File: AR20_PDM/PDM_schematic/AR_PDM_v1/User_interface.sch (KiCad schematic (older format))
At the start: 63 parts, among them P1 B4B-PH-SM4-TB, U32 Fet-P, U33 Fet-P, U34 Fet-P, U35 Fet-P, U36 Fet-P

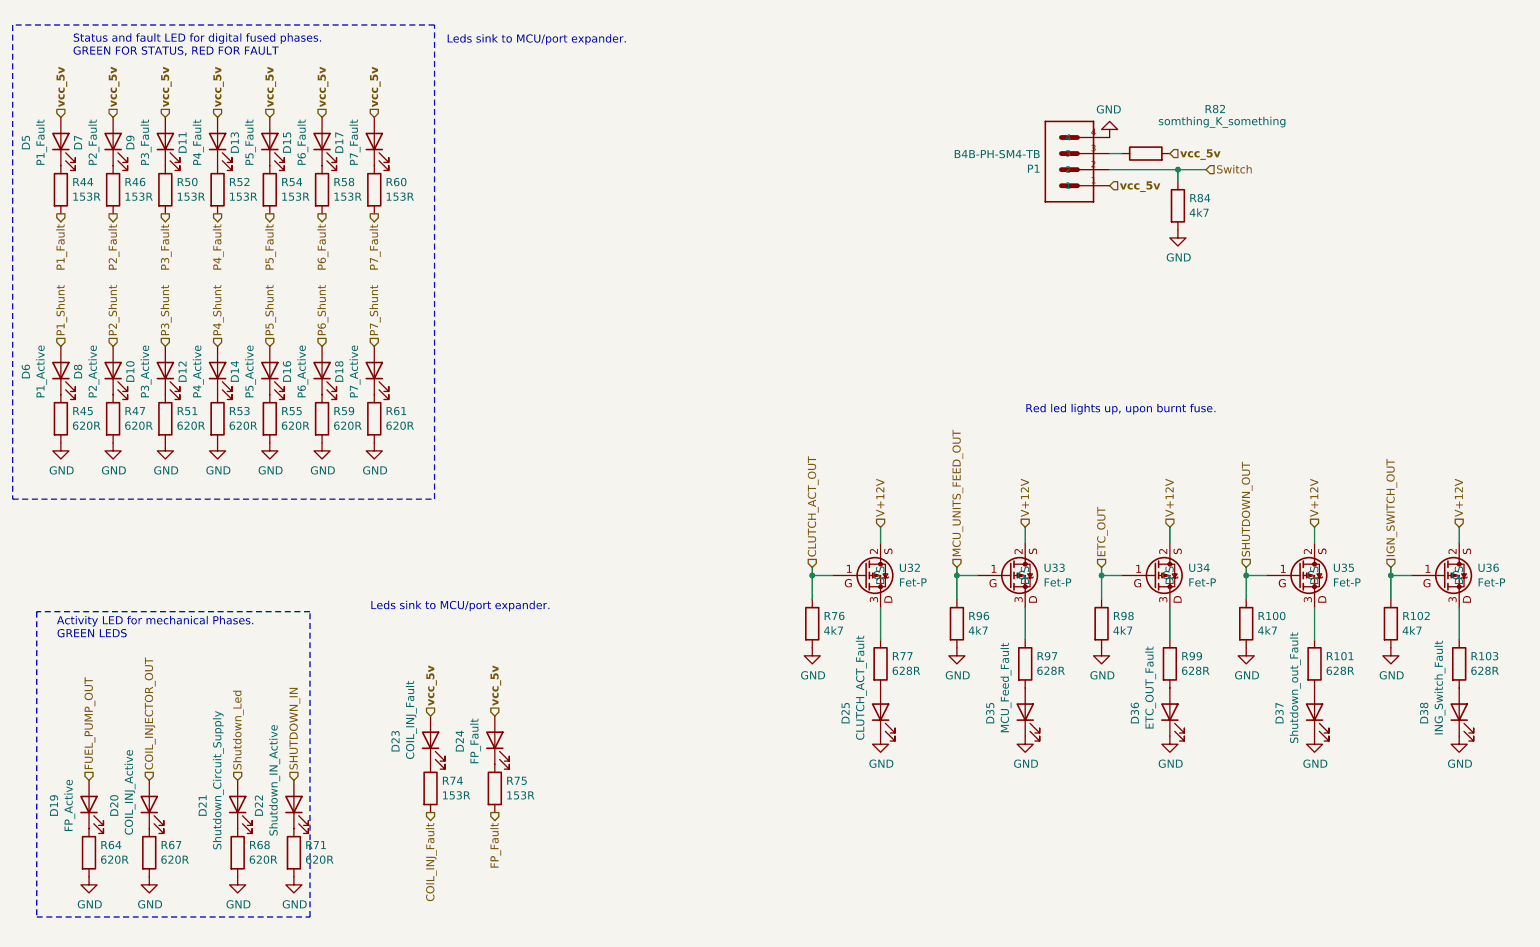
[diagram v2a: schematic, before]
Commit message: Further testing, reveals pdm needs rework
-  As of now, there are major errors in schematics.
- Needs rework. Version charlie postponed.
- Very nice pcb layout thats almost finished. 
   worth noting this layout for the future
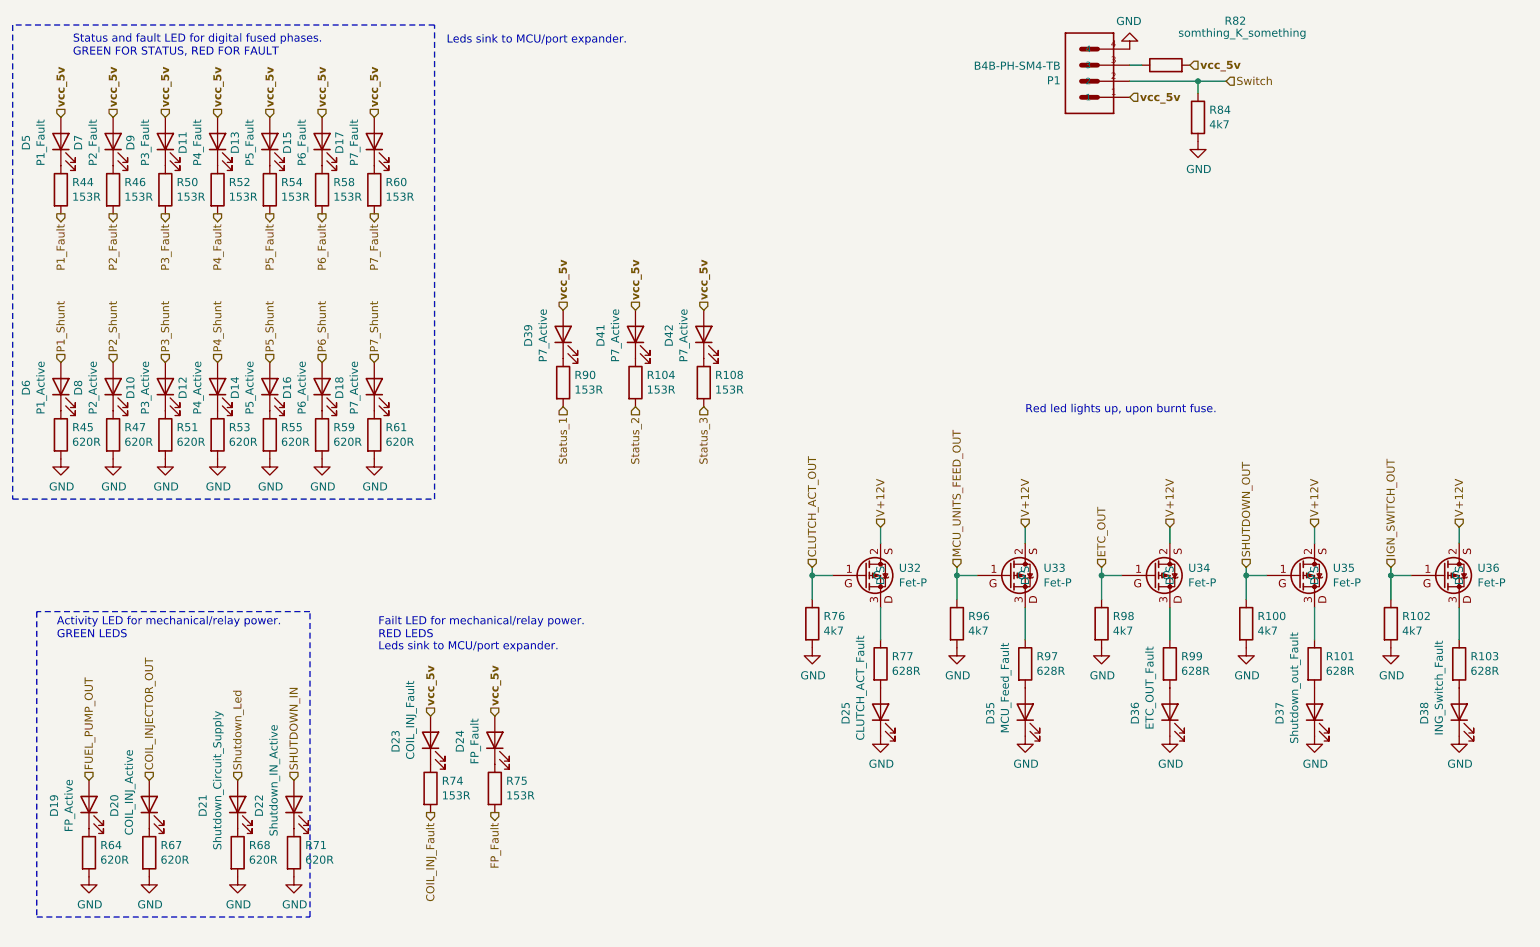
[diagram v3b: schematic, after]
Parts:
- added D39, D41, D42: P7_Active, LED_SMD:LED_1206_3216Metric, symbol Device:LED
- added R104, R108, R90: 153R, Resistor_SMD:R_0603_1608Metric, symbol AR20_PDM_v1-rescue:R-Device
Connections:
- net vcc_5v: now also D39.2 (A), D41.2 (A), D42.2 (A)
- new net: D39.1 (K), R90.1
- new net: D41.1 (K), R104.1
- new net: D42.1 (K), R108.1
- new net Status_1: R90.2
- new net Status_2: R104.2
- new net Status_3: R108.2
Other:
- note added: "Activity LED for mechanical/relay power.\nGREEN LEDS"
- note added: "Failt LED for mechanical/relay power.\nRED LEDS"
- note removed: "Activity LED for mechanical Phases. \nGREEN LEDS"
- moved on the sheet: D10, D12, D14, D16, D18, D6, D8, P1, R45, R47, R51, R53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

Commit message: Working on pcb layout
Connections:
- net P1_Shunt renamed P1_OUT
- net P2_Shunt renamed P2_OUT
- net P3_Shunt renamed P3_OUT
- net P4_Shunt renamed P4_OUT
- net P5_Shunt renamed P5_OUT
- net P6_Shunt renamed P6_OUT
- net P7_Shunt renamed P7_OUT
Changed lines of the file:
@@
 $EndComp
 Text HLabel 2175 3025 1    50   Input ~ 0
-P2_Shunt
+P2_OUT
 Text HLabel 2500 3025 1    50   Input ~ 0
-P3_Shunt
+P3_OUT
 Text HLabel 2825 3025 1    50   Input ~ 0
-P4_Shunt
+P4_OUT
 Text HLabel 3150 3025 1    50   Input ~ 0
-P5_Shunt
+P5_OUT
 Text HLabel 3475 3025 1    50   Input ~ 0
-P6_Shunt
+P6_OUT
 Text HLabel 3800 3025 1    50   Input ~ 0
-P7_Shunt
+P7_OUT
 Text HLabel 2950 5625 1    50   Input ~ 0
 Shutdown_Led
@@
 SHUTDOWN_IN
 Text HLabel 1850 3025 1    50   Input ~ 0
-P1_Shunt
+P1_OUT
 $Comp
 L AR20_PDM_v1-rescue:B4B-PH-SM4-TB P?

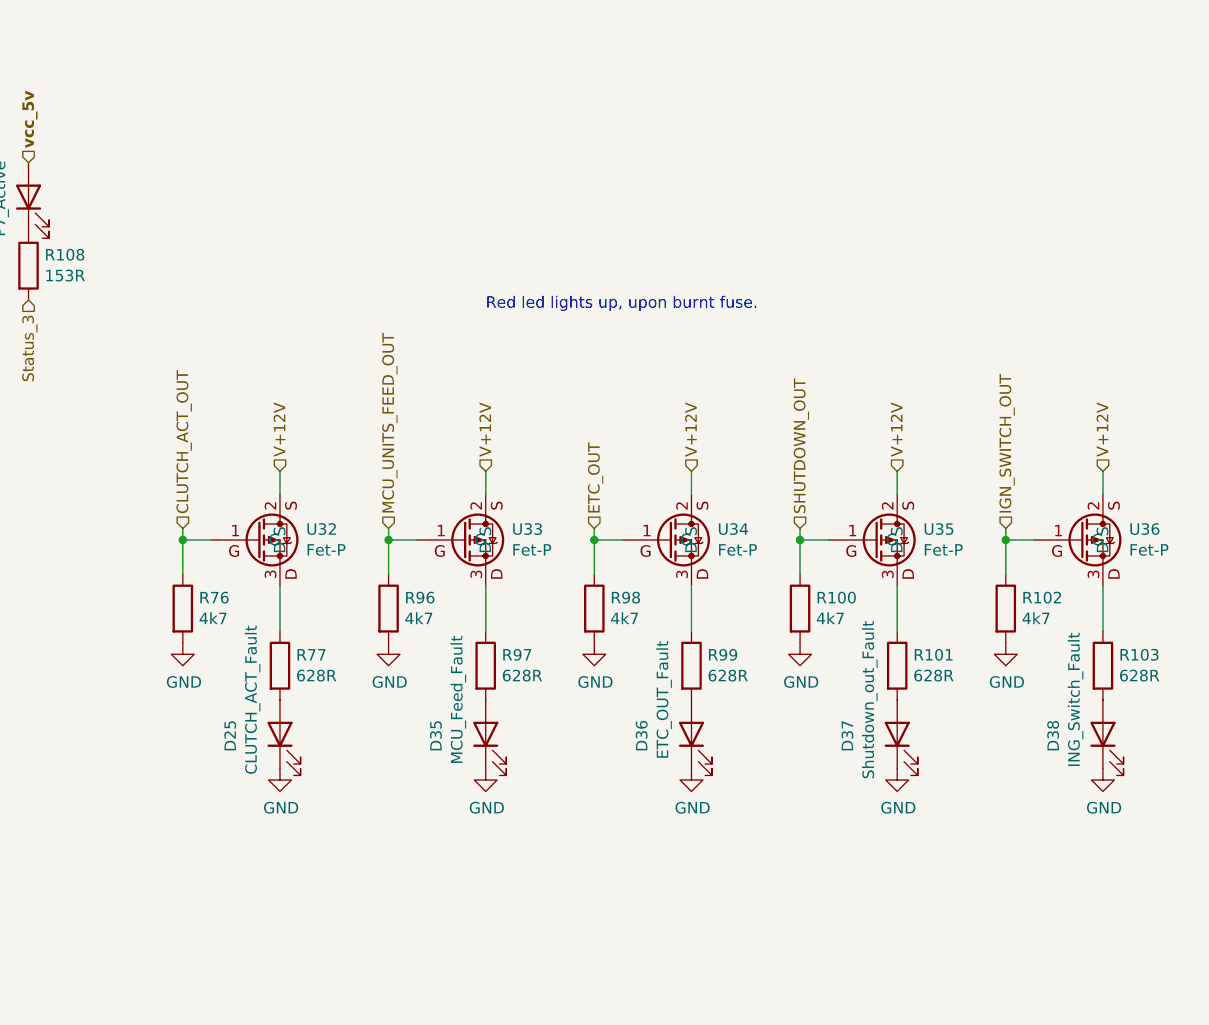
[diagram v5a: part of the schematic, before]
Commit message: PDM mostly complete
- Reverse polarity protection implemented
- All traces layed out
- final polish missing
- DRC missing
- Final check missing
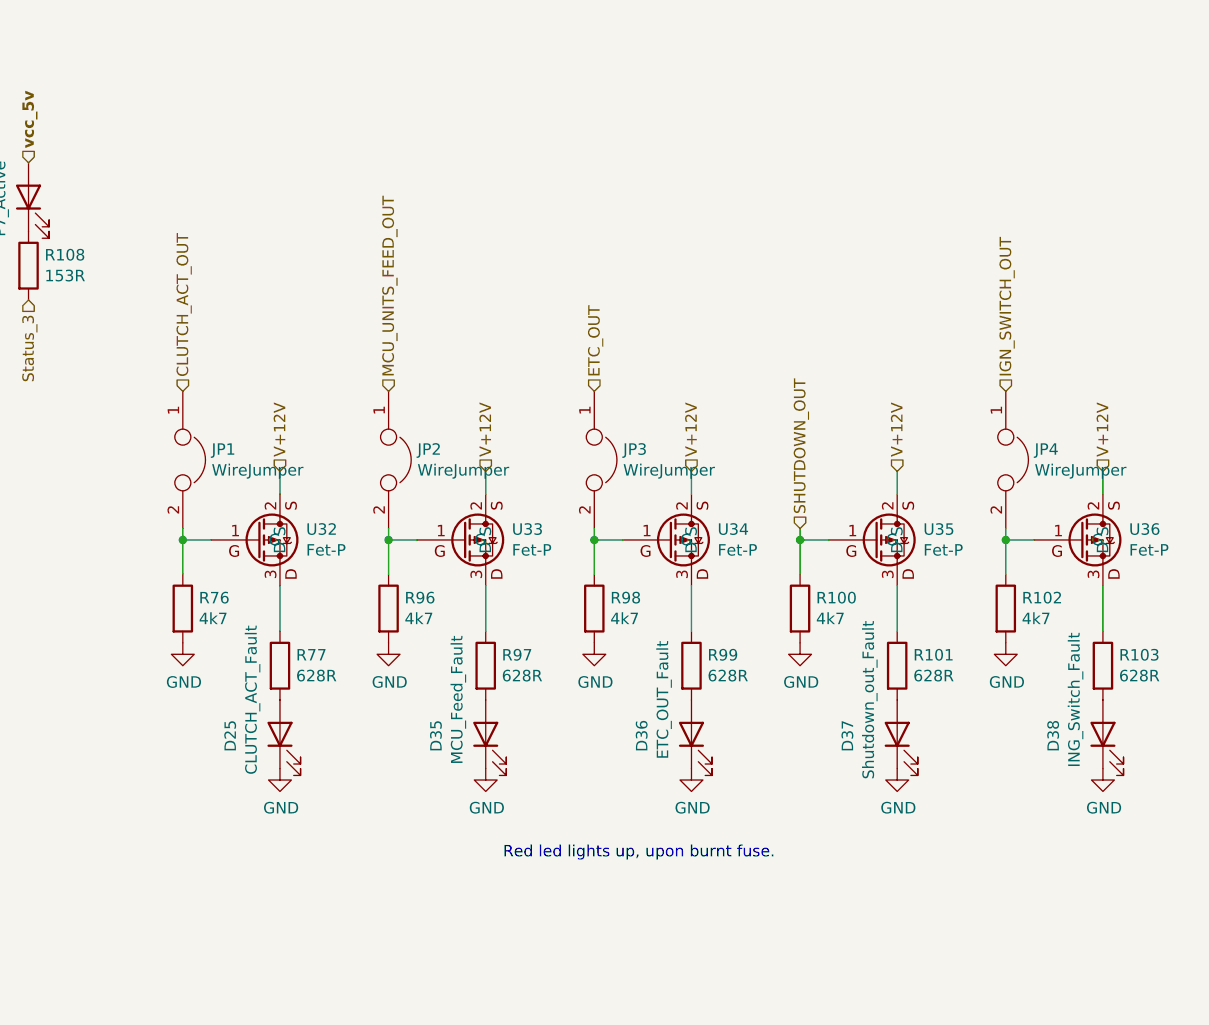
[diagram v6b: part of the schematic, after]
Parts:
- added JP1: WireJumper, AR_PDM_v1:WireJumper_15mm, symbol Device:Jumper
- added JP2: WireJumper, AR_PDM_v1:WireJumper_25mm, symbol Device:Jumper
- added JP3: WireJumper, AR_PDM_v1:WireJumper_20mm, symbol Device:Jumper
- added JP4: WireJumper, AR_PDM_v1:WireJumper_10.5mm, symbol Device:Jumper
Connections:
- net CLUTCH_ACT_OUT: now also JP1.1; no longer R76.1, U32.1 (G)
- net ETC_OUT: now also JP3.1; no longer R98.1, U34.1 (G)
- net IGN_SWITCH_OUT: now also JP4.1; no longer R102.1, U36.1 (G)
- net MCU_UNITS_FEED_OUT: now also JP2.1; no longer R96.1, U33.1 (G)
- new net: JP1.2, R76.1, U32.1 (G)
- new net: JP2.2, R96.1, U33.1 (G)
- new net: JP3.2, R98.1, U34.1 (G)
- new net: JP4.2, R102.1, U36.1 (G)
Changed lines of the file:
@@
 	0    -1   -1   0
 $EndComp
-Text HLabel 6525 4300 1    50   Input ~ 0
-CLUTCH_ACT_OUT
-Text HLabel 7425 4300 1    50   Input ~ 0
-MCU_UNITS_FEED_OUT
 Text HLabel 9100 1275 2    50   Input ~ 0
 Switch
@@
 	1    0    0    -1
 $EndComp
-Text HLabel 10125 4300 1    50   Input ~ 0
+Text HLabel 10125 3700 1    50   Input ~ 0
 IGN_SWITCH_OUT
 Text HLabel 9225 4300 1    50   Input ~ 0
 SHUTDOWN_OUT
-Text HLabel 8325 4300 1    50   Input ~ 0
+Text HLabel 8325 3700 1    50   Input ~ 0
 ETC_OUT
 Text Notes 3825 4825 0    50   ~ 0
 Leds sink to MCU/port expander.
-Text Notes 7850 3350 0    50   ~ 0
+Text Notes 7925 5750 0    50   ~ 0
 Red led lights up, upon burnt fuse.\n
 $Comp
@@
 	1    0    0    -1
 $EndComp
+$Comp
+L Device:Jumper JP?
+U 1 1 5F2E0BF8
+P 6525 4000
+AR Path="/5DA8920B/5F2E0BF8" Ref="JP?"  Part="1"
+AR Path="/5E5484EE/5F2E0BF8" Ref="JP1"  Part="1"
+F 0 "JP1" V 6479 4126 50  0000 L CNN
+F 1 "WireJumper" V 6570 4126 50  0000 L CNN
+F 2 "AR_PDM_v1:WireJumper_15mm" H 6525 4000 50  0001 C CNN
+F 3 "~" H 6525 4000 50  0001 C CNN
+	1    6525 4000
+	0    1    1    0
+$EndComp
+Text HLabel 6525 3700 1    50   Input ~ 0
+CLUTCH_ACT_OUT
+Text HLabel 7425 3700 1    50   Input ~ 0
+MCU_UNITS_FEED_OUT
+$Comp
+L Device:Jumper JP?
+U 1 1 5F2E7F62
+P 7425 4000
+AR Path="/5DA8920B/5F2E7F62" Ref="JP?"  Part="1"
+AR Path="/5E5484EE/5F2E7F62" Ref="JP2"  Part="1"
+F 0 "JP2" V 7379 4126 50  0000 L CNN
+F 1 "WireJumper" V 7470 4126 50  0000 L CNN
+F 2 "AR_PDM_v1:WireJumper_25mm" H 7425 4000 50  0001 C CNN
+F 3 "~" H 7425 4000 50  0001 C CNN
+	1    7425 4000
+	0    1    1    0
+$EndComp
+$Comp
+L Device:Jumper JP?
+U 1 1 5F2E8AB1
+P 8325 4000
+AR Path="/5DA8920B/5F2E8AB1" Ref="JP?"  Part="1"
+AR Path="/5E5484EE/5F2E8AB1" Ref="JP3"  Part="1"
+F 0 "JP3" V 8279 4126 50  0000 L CNN
+F 1 "WireJumper" V 8370 4126 50  0000 L CNN
+F 2 "AR_PDM_v1:WireJumper_20mm" H 8325 4000 50  0001 C CNN
+F 3 "~" H 8325 4000 50  0001 C CNN
+	1    8325 4000
+	0    1    1    0
+$EndComp
+$Comp
+L Device:Jumper JP?
+U 1 1 5F2E9501
+P 10125 4000
+AR Path="/5DA8920B/5F2E9501" Ref="JP?"  Part="1"
+AR Path="/5E5484EE/5F2E9501" Ref="JP4"  Part="1"
+F 0 "JP4" V 10079 4126 50  0000 L CNN
+F 1 "WireJumper" V 10170 4126 50  0000 L CNN
+F 2 "AR_PDM_v1:WireJumper_10.5mm" H 10125 4000 50  0001 C CNN
+F 3 "~" H 10125 4000 50  0001 C CNN
+	1    10125 4000
+	0    1    1    0
+$EndComp
 $EndSCHEMATC
